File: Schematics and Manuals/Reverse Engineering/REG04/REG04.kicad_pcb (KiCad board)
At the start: 2 copper layers, 105.8 x 128.5 mm, 203 parts, among them J1 Conn_01x02_Pin, J10 Conn_01x02_Pin, J11 Conn_01x02_Pin, J12 Conn_01x02_Pin, J13 Conn_01x02_Pin, J14 Conn_01x02_Pin, J15 Conn_01x02_Pin, J16 Conn_01x02_Pin, J17 Conn_01x02_Pin, J18 Conn_01x02_Pin, J19 Conn_01x02_Pin, J2 Conn_01x02_Pin, J20 Conn_01x02_Pin, J21 Conn_01x02_Pin, J22 Conn_01x02_Pin, J23 Conn_01x02_Pin, J24 Conn_01x02_Pin, J25 Conn_01x02_Pin, J26 Conn_01x02_Pin, J27 Conn_01x02_Pin, J28 Conn_01x02_Pin, J29 Conn_01x02_Pin, J3 Conn_01x02_Pin, J30 Conn_01x02_Pin, J31 Conn_01x02_Pin, J32 Conn_01x02_Pin, J33 Conn_01x02_Pin, J34 Conn_01x02_Pin, J35 Conn_01x02_Pin, J36 Conn_01x02_Pin, J37 Conn_01x02_Pin, J38 Conn_01x02_Pin, J39 Conn_01x02_Pin, J4 Conn_01x02_Pin, J40 Conn_01x02_Pin, J5 Conn_01x02_Pin, J6 Conn_01x02_Pin, J7 Conn_01x02_Pin, J8 Conn_01x02_Pin, J9 Conn_01x02_Pin, Q1 Q_PNP_EBC, Q10 Q_PNP_EBC, Q11 Q_PNP_EBC, Q12 Q_PNP_EBC, Q13 Q_PNP_EBC, Q14 Q_PNP_EBC, Q15 Q_PNP_EBC, Q16 Q_PNP_EBC, Q2 Q_PNP_EBC, Q3 Q_PNP_EBC, Q4 Q_PNP_EBC, Q5 Q_PNP_EBC, Q6 Q_PNP_EBC, Q7 Q_PNP_EBC, Q8 Q_PNP_EBC, Q9 Q_PNP_EBC

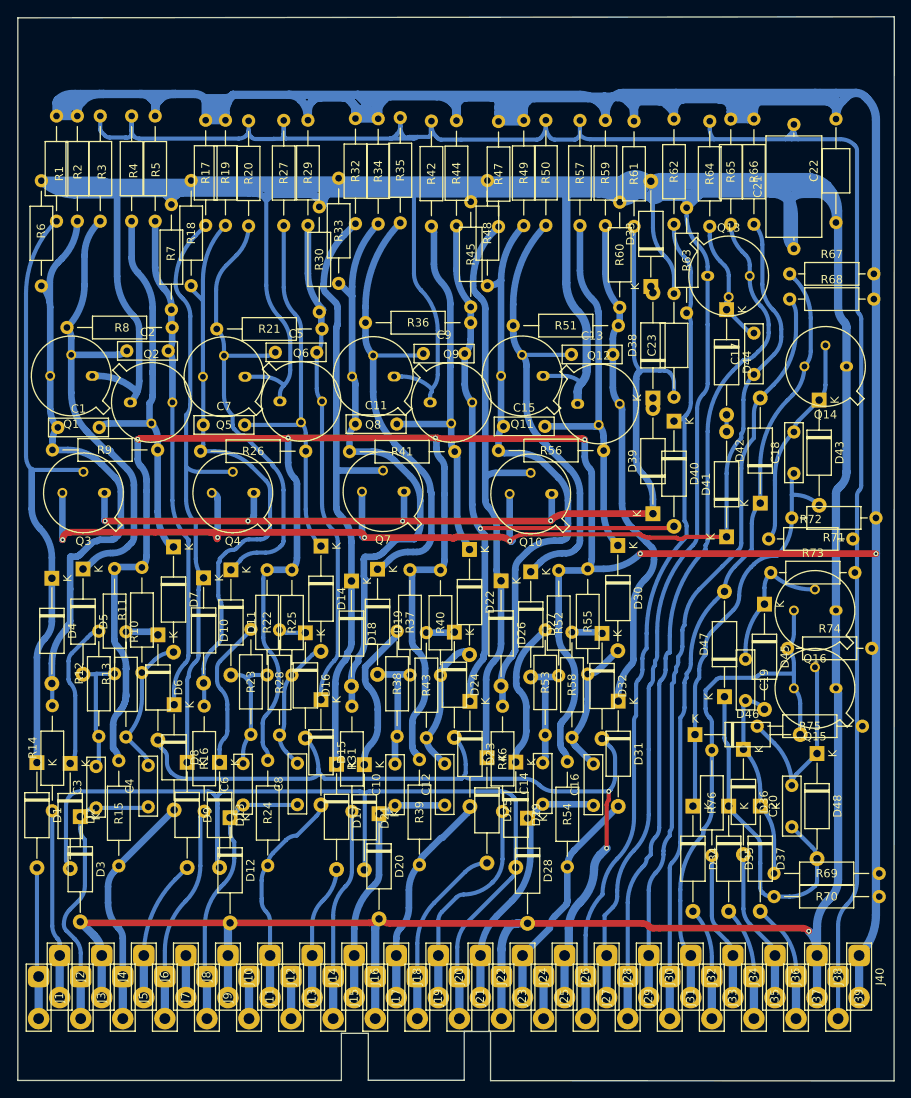
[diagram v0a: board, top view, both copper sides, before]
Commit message: Complete renumbering and reordering of the schematic and PCB
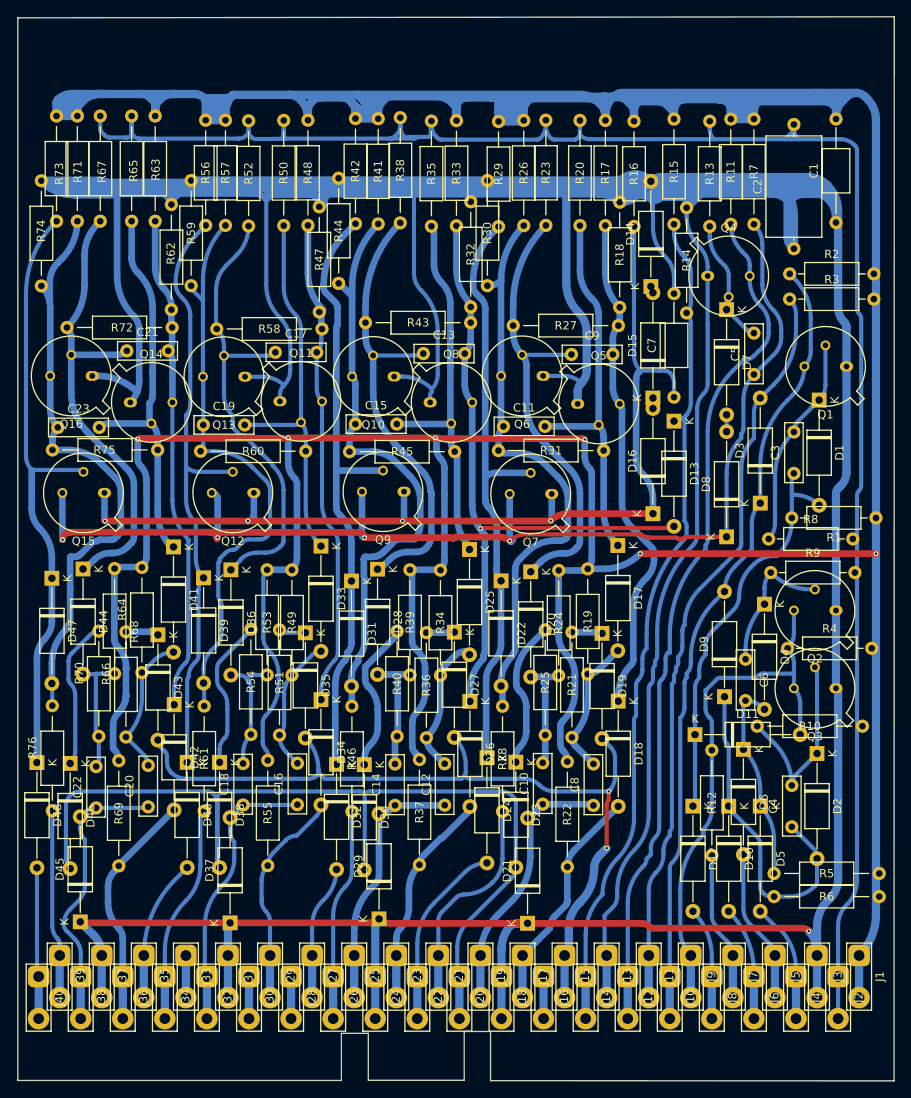
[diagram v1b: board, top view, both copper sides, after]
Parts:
- R46: renamed from R31; value R -> 10k
- R61: renamed from R16; value R -> 10k
- moved D21 12.7 mm to (159.6, 142.2), turned to 90 degrees
- moved D29 12.7 mm to (141.7, 141.6), turned to 90 degrees
- moved D37 12.7 mm to (123.7, 142.1), turned to 90 degrees
- moved D45 12.7 mm to (105.6, 142.0), turned to 90 degrees
- renumbered C22 to C1, C14 to C10, C15 to C11, C9 to C13, C10 to C14, C11 to C15, C8 to C16, C5 to C17, C6 to C18, C7 to C19, C21 to C2, C4 to C20, C2 to C21, C3 to C22, C1 to C23, C18 to C3, C20 to C4, C17 to C5, C19 to C6, C23 to C7, C16 to C8, C13 to C9, D43 to D1, D35 to D10, D46 to D11, D34 to D12, D40 to D13, D33 to D14, D38 to D15, D39 to D16, D30 to D17, D31 to D18, D32 to D19, D48 to D2, D27 to D20, D28 to D21, D26 to D22, D29 to D23, D25 to D24, D22 to D25, D23 to D26, D24 to D27, D19 to D28, D20 to D29, D42 to D3, D21 to D30, D18 to D31, D17 to D32, D14 to D33, D15 to D34, D16 to D35, D11 to D36, D12 to D37, D13 to D38, D10 to D39, D45 to D4, D9 to D40, D7 to D41, D8 to D42, D6 to D43, D5 to D44, D3 to D45, D2 to D46, D4 to D47, D1 to D48, D37 to D5, D36 to D6, D44 to D7, D41 to D8, D47 to D9, J40 to J1, J31 to J10, J30 to J11, J29 to J12, J28 to J13, J27 to J14, J26 to J15, J25 to J16, J24 to J17, J23 to J18, J22 to J19, J39 to J2, J21 to J20, J20 to J21, J19 to J22, J18 to J23, J17 to J24, J16 to J25, J15 to J26, J14 to J27, J13 to J28, J12 to J29, J38 to J3, J11 to J30, J10 to J31, J9 to J32, J8 to J33, J7 to J34, J6 to J35, J5 to J36, J4 to J37, J3 to J38, J2 to J39, J37 to J4, J1 to J40, J36 to J5, J35 to J6, J34 to J7, J33 to J8, J32 to J9, Q14 to Q1, Q8 to Q10, Q6 to Q11, Q4 to Q12, Q5 to Q13, Q2 to Q14, Q3 to Q15, Q1 to Q16, Q16 to Q2, Q15 to Q3, Q13 to Q4, Q12 to Q5, Q11 to Q6, Q10 to Q7, Q9 to Q8, Q7 to Q9, R71 to R1, R75 to R10, R65 to R11, R76 to R12, R64 to R13, R63 to R14, R62 to R15, R61 to R16, R59 to R17, R60 to R18, R55 to R19, R67 to R2, R57 to R20, R58 to R21, R54 to R22, R50 to R23, R52 to R24, R53 to R25, R49 to R26, R51 to R27, R46 to R28, R47 to R29, R68 to R3, R48 to R30, R56 to R31, R45 to R32, R44 to R33, R40 to R34, R42 to R35, R43 to R36, R39 to R37, R35 to R38, R37 to R39, R74 to R4, R38 to R40, R34 to R41, R32 to R42, R36 to R43, R33 to R44, R41 to R45, R30 to R47, R29 to R48, R25 to R49, R69 to R5, R27 to R50, R28 to R51, R20 to R52, R22 to R53, R23 to R54, R24 to R55, R17 to R56, R19 to R57, R21 to R58, R18 to R59, R70 to R6, R26 to R60, R7 to R62, R5 to R63, R11 to R64, R4 to R65, R13 to R66, R3 to R67, R10 to R68, R15 to R69, R66 to R7, R12 to R70, R2 to R71, R8 to R72, R1 to R73, R6 to R74, R9 to R75, R14 to R76, R72 to R8, R73 to R9
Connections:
- net /~{Gout} renamed /~{BUS-OUT}
- net P1 renamed P40-FF1-~{Q}EN
- net P12 renamed P29-FF2-~{S}
- net P14 renamed P27-FF3-~{Q}EN
- net P15 renamed P26-FF3-~{Q}Z
- net P18 renamed P23-FF3-~{S}
- net P19 renamed P22-FF4-~{Q}EN
- net P2 renamed P39-FF1-~{Q}Z
- net P20 renamed P21-FF4-~{Q}Z
- net P21 GRset renamed P20-BUS-~{RES}
- net P24 renamed P17-FF4-~{S}
- net P26 Gset renamed P15-BUS-~{SET}
- net P27 renamed P14-FF3-Q
- net P29 Gout renamed P12-BUS-OUT
- net P30 A renamed P11-FF5-SEN
- net P31 IO renamed P10-FF5-Q
- net P32 Out renamed P9-FF5-~{Q}
- net P33 B renamed P8-FF5-~{S}
- net P34 OutZ renamed P7-FF5-~{Q}Z
- net P35 C renamed P6-FF5-~{R}
- net P36 D renamed P5-FF5-~{REN2}
- net P37 E renamed P4-FF5-~{REN1}
- net P5 renamed P36-FF1-~{S}
- net P6 renamed P35-FF2-~{Q}EN
- net P7 renamed P34-FF2-~{Q}Z
- C10 pad 1: P22 -1V -> P19-FF4-~{CLK}
- C10 pad 2: Net-(D27-A) -> Net-(D20-A)
- C12 pad 1: P16 -1V -> Net-(D25-A)
- C12 pad 2: Net-(D22-A) (its old number) -> P25-FF3-~{CLK}
- C14 pad 1: P16 -1V -> P25-FF3-~{CLK}
- C14 pad 2: Net-(D19-A) -> Net-(D28-A)
- C16 pad 1: P9 -1V -> P32-FF2-~{CLK}
- C18 pad 1: P9 -1V -> P32-FF2-~{CLK}
- C18 pad 2: Net-(D11-A) -> Net-(D36-A)
- C20 pad 1: P3 -1V -> P38-FF1-~{CLK}
- C22 pad 1: P3 -1V -> P38-FF1-~{CLK}
- C8 pad 1: P22 -1V -> P19-FF4-~{CLK}
- D20 pad 2: Net-(D27-A) -> Net-(D20-A)
- D21 pad 1: P22 -1V -> GND
- D21 pad 2: GND -> P19-FF4-~{CLK}
- D25 pad 2: Net-(D22-A) (its old number) -> Net-(D25-A)
- D28 pad 2: Net-(D19-A) -> Net-(D28-A)
- D29 pad 1: P16 -1V -> GND
- D29 pad 2: GND -> P25-FF3-~{CLK}
- D36 pad 2: Net-(D11-A) -> Net-(D36-A)
- D37 pad 1: P9 -1V -> GND
- D37 pad 2: GND -> P32-FF2-~{CLK}
- D45 pad 1: P3 -1V -> GND
- D45 pad 2: GND -> P38-FF1-~{CLK}
- J19 pad 1: P22 -1V -> P19-FF4-~{CLK}
- J19 pad 2: P22 -1V -> P19-FF4-~{CLK}
- J25 pad 1: P16 -1V -> P25-FF3-~{CLK}
- J25 pad 2: P16 -1V -> P25-FF3-~{CLK}
- J32 pad 1: P9 -1V -> P32-FF2-~{CLK}
- J32 pad 2: P9 -1V -> P32-FF2-~{CLK}
- J38 pad 1: P3 -1V -> P38-FF1-~{CLK}
- J38 pad 2: P3 -1V -> P38-FF1-~{CLK}
- R24 pad 1: -12V -> Net-(D20-A)
- R24 pad 2: Net-(D27-A) -> -12V
- R25 pad 1: Net-(D27-A) -> Net-(D20-A)
- R34 pad 1: Net-(D22-A) (its old number) -> Net-(D25-A)
- R36 pad 1: Net-(D22-A) (its old number) -> Net-(D25-A)
- R39 pad 1: -12V -> Net-(D28-A)
- R39 pad 2: Net-(D19-A) -> -12V
- R40 pad 1: Net-(D19-A) -> Net-(D28-A)
- R53 pad 1: -12V -> Net-(D36-A)
- R53 pad 2: Net-(D11-A) -> -12V
- R54 pad 1: Net-(D11-A) -> Net-(D36-A)
- R59 pad 2: GND -> unconnected-(R59-Pad2)
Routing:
- net P38-FF1-~{CLK}: track 0.00 -> 34.6 mm
- net P3 -1V: track 34.6 -> 0.00 mm
- net P9 -1V: track 34.2 -> 0.00 mm
- net P32-FF2-~{CLK}: track 0.00 -> 34.2 mm
- net P22 -1V: track 32.2 -> 0.00 mm
- net P19-FF4-~{CLK}: track 0.00 -> 32.2 mm
- net P25-FF3-~{CLK}: track 0.00 -> 31.3 mm
- net P16 -1V: track 31.3 -> 0.00 mm
- net Net-(D25-A): track 0.00 -> 16.8 mm
- net Net-(D22-A) (its old number): track 16.8 -> 0.00 mm
- net Net-(D36-A): track 0.00 -> 15.2 mm
- net Net-(D11-A): track 15.2 -> 0.00 mm
- net Net-(D28-A): track 0.00 -> 14.8 mm
- net Net-(D19-A): track 14.8 -> 0.00 mm
- net Net-(D27-A): track 13.9 -> 0.00 mm
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
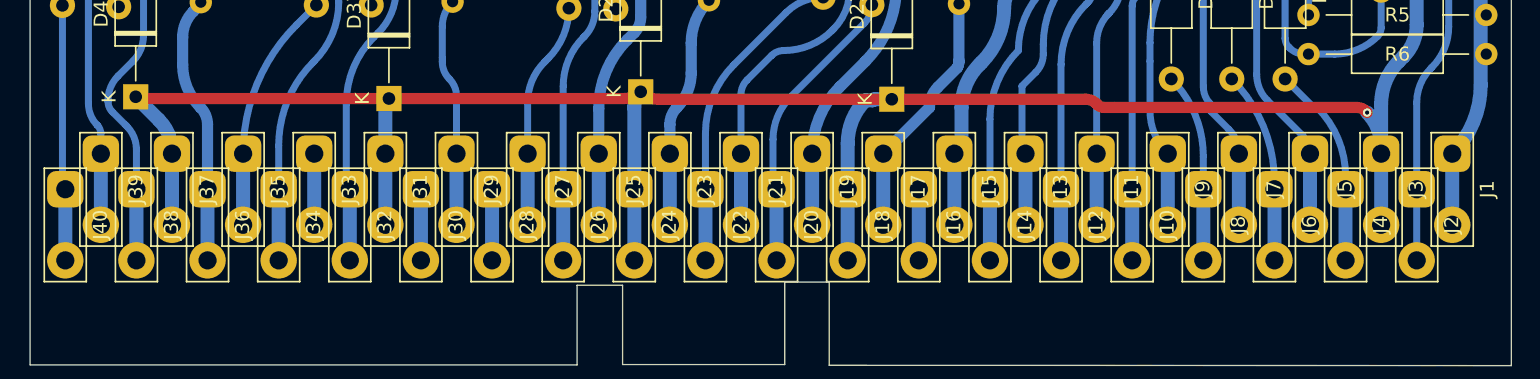
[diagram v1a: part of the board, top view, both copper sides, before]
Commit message: Replaced connector for the standard connector and created a PCB part for the 40 pin ELCO like connector
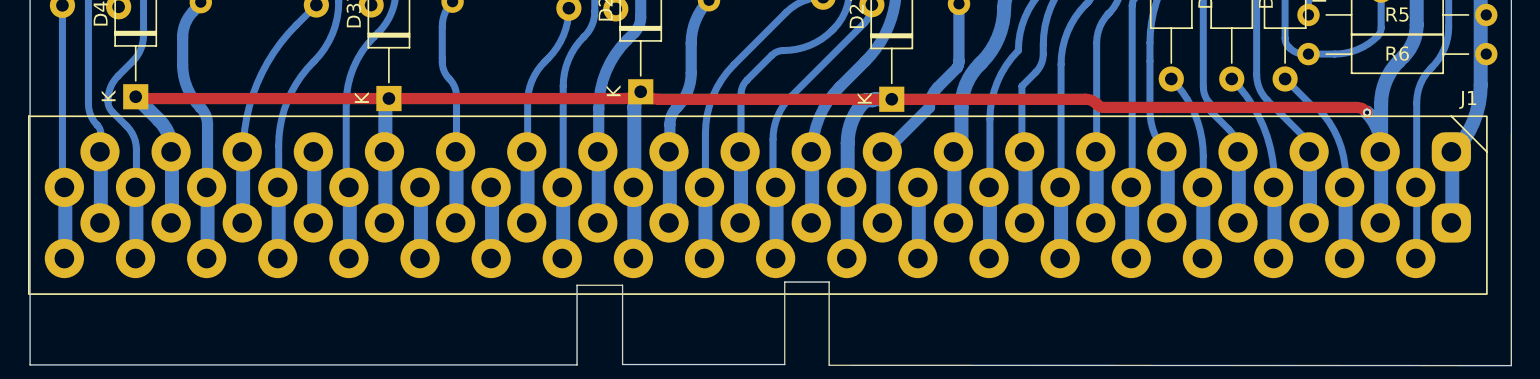
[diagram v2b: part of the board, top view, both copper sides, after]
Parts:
- removed J10, J11, J12, J13, J14, J15, J16, J17, J18, J19, J2, J20, J21, J22, J23, J24, J25, J26, J27, J28, J29, J3, J30, J31, J32, J33, J34, J35, J36, J37, J38, J39, J4, J40, J5, J6, J7, J8, J9: Conn_01x02_Pin, TestPoint:TestPoint_2Pads_Pitch5.08mm_Drill1.3mm
- J1: value Conn_01x02_Pin -> Conn_01x40; footprint TestPoint:TestPoint_2Pads_Pitch5.08mm_Drill1.3mm -> Logi620:ELCO 40
- moved J1 0.14 mm to (199.6, 145.9), turned to 0 degrees
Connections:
- net /~{BUS-OUT} renamed ~{BUS-OUT}
- J1 pad 2: -12V -> +6V
- R59 pad 2: unconnected-(R59-Pad2) -> GND
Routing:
- net (no net): track 0.00 -> 20.3 mm
- net unconnected-(J33-Pin_1-Pad1): track 5.08 -> 0.00 mm
- net unconnected-(J30-Pin_1-Pad1): track 5.08 -> 0.00 mm
- net unconnected-(J28-Pin_1-Pad1): track 5.08 -> 0.00 mm
- net unconnected-(J16-Pin_1-Pad1): track 5.08 -> 0.00 mm
